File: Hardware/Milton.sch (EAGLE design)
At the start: 80 parts, among them Q1 12MHz, U10 MAX31850K, U2 DDC113TU-7-F, U3 USD-SOCKETNEW, U4 MMA8452Q, U5 TCR2EE50,LM, U6 SI4464, U7 TPS61200, U8 BME280, X1 B4B-ZR, X2 M023.5MM

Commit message: Update
Continue cleaning up traces and adding part numbers
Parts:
- removed C46: 100pF, SparkFun-Capacitors:CAP0603-CAP
- removed C47: 0.1uF, SparkFun-Capacitors:CAP0603-CAP
- removed C48: 1uF, SparkFun-Capacitors:CAP0603-CAP
- removed JP5: M02JST-PTH-2, SparkFun-Connectors:M02JST-PTH-2
- removed L8: SRN3015-2R2M, wrea:SRN3015-2R2M
- removed R15: 4.7k, SparkFun-Resistors:RESISTOR0603
- removed U$5: USB-CON-5PIN-105017-0001, GeekAmmo:USB-CON-5PIN-105017-0001
- added C21: 0.1uF, SparkFun-Capacitors:CAP0805
- added C33: 36pF, SparkFun-Capacitors:CAP0603-CAP
- added C34: 1000pF, SparkFun:CAP0805
- added JP2: (no value), SparkFun-Connectors:M03PTH
- added L3: 220nH, SparkFun-Passives:INDUCTOR0603
- added R12: 1k, SparkFun-Resistors:RESISTOR0603
- added U9: BME280, wrea:BME280
- C1: value 0.1uF -> 47pF; device SparkFun-Capacitors:CAP0805 -> SparkFun-Capacitors:CAP0603-CAP; MPN CL10B104KO8NNNC -> CL10C470JB8NCNC
- C10: value 0.1uF -> 10uF; device SparkFun-Capacitors:CAP0603-CAP -> SparkFun-Capacitors:10UF-TANT; MPN CL10B104KO8NNNC -> F931A106KAA
- C11: device SparkFun-Capacitors:CAP0603-CAP -> SparkFun:CAP0603-CAP
- C12: device SparkFun-Capacitors:10UF-TANT -> SparkFun-Capacitors:CAP0805; MPN F931A106KAA -> GRM21BR61C106KE15L
- C13: device SparkFun-Capacitors:CAP0805 -> SparkFun-Capacitors:CAP0603-CAP
- C14: value 100pF -> 10uF; device SparkFun-Capacitors:CAP0603-CAP -> SparkFun-Capacitors:CAP0805; MPN CL10B101KB8NNNC -> GRM21BR61C106KE15L
- C15: value 56pF -> 0.1uF; MPN CL10C560JB8NNNC -> CL10B104KO8NNNC
- C16: value 36pF -> 0.1uF; MPN GRM1885C1H360JA01D -> CL10B104KO8NNNC
- C17: value 22pF -> 0.1uF; device SparkFun:CAP0805 -> SparkFun-Capacitors:CAP0805; MPN C1608C0G1H220J080AA -> CL10B104KO8NNNC
- C18: value 10uF -> 4.7uF; device SparkFun-Capacitors:CAP0805 -> SparkFun-Capacitors:CAP0603-CAP; MPN GRM21BR61C106KE15L -> CC0603KRX5R6BB475
- C19: device SparkFun-Capacitors:CAP0603-CAP -> SparkFun-Capacitors:CAP0805
- C2: value 56pF -> 47pF; MPN CL10C560JB8NNNC -> CL10C470JB8NCNC
- C20: value 10uF -> 0.1uF; MPN GRM21BR61C106KE15L -> CL10B104KO8NNNC
- C22: value 0.1uF -> 100pF; MPN CL10B104KO8NNNC -> CL10B101KB8NNNC
- C23: value 1000pF -> 1uF; device SparkFun:CAP0805 -> SparkFun-Capacitors:CAP0603-CAP; MPN C0603C102J5RACTU -> CL10B105KP8NNNC
- C24: value 1000pF -> 0.1uF; MPN C0603C102J5RACTU -> CL10B104KO8NNNC
- C25: value 47pF -> 100pF; MPN CL10C470JB8NCNC -> CL10B101KB8NNNC
- C26: value 47pF -> 22pF; device SparkFun-Capacitors:CAP0603-CAP -> SparkFun:CAP0805; MPN CL10C470JB8NCNC -> C1608C0G1H220J080AA
- C27, C28: value 0.1uF -> 1000pF; device SparkFun-Capacitors:CAP0805 -> SparkFun-Capacitors:CAP0603-CAP; MPN CL10B104KO8NNNC -> C0603C102J5RACTU
- C29: value 4.7uF -> 12pF; MPN CC0603KRX5R6BB475 -> CL10C120JB8NNNC
- C3: device SparkFun:CAP0603-CAP -> SparkFun-Capacitors:CAP0603-CAP
- C30: value 12pF -> 36pF; MPN CL10C120JB8NNNC -> GRM1885C1H360JA01D
- C31: value 1000pF -> 56pF; MPN C0603C102J5RACTU -> CL10C560JB8NNNC
- C32: value 0.1uF -> 56pF; MPN CL10B104KO8NNNC -> CL10C560JB8NNNC
- C4: value 36pF -> 18pF; device SparkFun-Capacitors:CAP0603-CAP -> SparkFun-Capacitors:CAP0805; MPN GRM1885C1H360JA01D -> C0603C180K3GACTU
- C6: value 18pF -> 0.1uF; device SparkFun-Capacitors:CAP0805 -> SparkFun-Capacitors:CAP0603-CAP; MPN C0603C180K3GACTU -> CL10B104KO8NNNC
- FB1, FB2: value (none) -> FB; device LoganSmith-Inductors:FB-1K-100MHZ-0603 -> SparkFun-Passives:FB; MPN (none) -> BLM18PG471SN1D
- JP1: value (none) -> M02JST-PTH-2; device SparkFun-Connectors:M04PTH -> SparkFun-Connectors:M02JST-PTH-2; MPN (none) -> S2B-PH-K-S(LF)(SN)
- JP3: device SparkFun-Connectors:M03PTH -> SparkFun-Connectors:M04PTH
- L1: value 68nH -> SRN3015-2R2M; device SparkFun-Passives:INDUCTOR0603 -> wrea:SRN3015-2R2M; MPN LQW18AN68NG00D -> SRN3015-4R7M
- L2: value 72nH -> 470nH; MPN LQW18AN72NG00D -> L0603CR47JRMST
- L4: value 68nH -> 150nH; MPN LQW18AN68NG00D -> LQW18ANR15G00D
- L5: value 470nH -> 68nH; MPN L0603CR47JRMST -> LQW18AN68NG00D
- L6: value 220nH -> 72nH; MPN LQW18ANR22G00D -> LQW18AN72NG00D
- L7: value 150nH -> 68nH; MPN LQW18ANR15G00D -> LQW18AN68NG00D
- R1: value 27 -> 4.7k; MPN MCR03ERTJ270 -> ESR03EZPJ472
- R11: value 180k -> 4.7k; MPN RC1608F184CS -> ERJ-3GEYJ472V
- R2: value 27 -> 10k; MPN MCR03ERTJ270 -> ESR03EZPJ103
- R3: value 4.7k -> 27; MPN ESR03EZPJ472 -> MCR03ERTJ270
- R4: value 1k -> 27; MPN RMCF0603JT1K00 -> MCR03ERTJ270
- R5: value 4.7k -> 10K; MPN ERJ-3GEYJ472V -> ESR03EZPJ103
- R6: value 4.7k -> 1M; MPN ERJ-3GEYJ472V -> MCT06030C1004FP500
- R7: value 10k -> 180k; MPN ESR03EZPJ103 -> RC1608F184CS
- R8: value 10K -> 4.7k; MPN ESR03EZPJ103 -> ERJ-3GEYJ472V
- R9: value 1M -> 4.7k; MPN MCT06030C1004FP500 -> ERJ-3GEYJ472V
- U$1: value 1575AT43A40 -> USB-MICRO_105017-0001; device ava:JTI_ANTENNA-1575AT43A40 -> wrea:USB-MICRO_105017-0001; MPN 1575AT43A0040E -> 105017-0001
- U$2: value UBLOX_MAX -> 1575AT43A40; device ava:UBLOX_MAX -> ava:JTI_ANTENNA-1575AT43A40; MPN MAX-7C-0 -> 1575AT43A0040E
- U$3: value FT231XQ-R -> UBLOX_MAX; device ftdi_ft231xq-r:FT231XQ-R -> ava:UBLOX_MAX; MPN (none) -> MAX-7C-0
- U1: value (none) -> FT231X; device microbuilder:LPC1768 -> wrea:FT231X; MPN LPC1768FBD100,551 -> FT231XQ-R
- U10: value MAX31850K -> SI4464; device LoganSmith-Analog_IC:MAX31850K -> ava:SI4464; MPN MAX31850TATB+ -> SI4464-B1B-FM
- U2: value DDC113TU-7-F -> (none); device wrea:DDC113TU-7-F -> microbuilder:LPC1768; MPN DDC113TU-7-F -> LPC1768FBD100,551
- U4: value MMA8452Q -> DDC113TU-7-F; device SparkFun-Sensors:MMA8452Q -> wrea:DDC113TU-7-F; MPN MMA8452QT -> DDC113TU-7-F
- U5: value TCR2EE50,LM -> TPS61200; device Xevelabs:IC_TCR2EEESV -> texas:TPS61200; MPN (none) -> TPS61200DRCR
- U6: value SI4464 -> TCR2EE50,LM; device ava:SI4464 -> Xevelabs:IC_TCR2EEESV; MPN SI4464-B1B-FM -> (none)
- U7: value TPS61200 -> MMA8452Q; device texas:TPS61200 -> SparkFun-Sensors:MMA8452Q; MPN TPS61200DRCR -> MMA8452QT
- U8: value BME280 -> MAX31850K; device wrea:BME280 -> LoganSmith-Analog_IC:MAX31850K; MPN (none) -> MAX31850TATB+
- X2: MPN (none) -> ED555/2DS
- renumbered J$3 to J$1, R18 to R13
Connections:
- removed net RSTOUT: U1.RSTOUT
- removed net RTCK: U1.RTCK
- removed net RXD1: U$2.2_TXD1, U1.P2[1]/PWM1[2]/RXD1
- removed net TCK: U1.TCK/SWDCLK
- removed net TDI: U1.TDI
- removed net TDO: U1.TDO/SWO
- removed net TMS: U1.TMS/SWDIO
- removed net TXD1: U$2.3_RXD1, U1.P2[0]/PWM1[1]/TXD1
- net 3.3V: now also C10.+, C11.1, C14.1, C16.1, C17.1, C18.1, C21.1, C23.1, C24.1, C25.1, C27.2, C6.2, C7.2, JP2.3, JP3.4, L2.1, R11.2, U$3.6_V_BCKP, U$3.7_VCC_IO, U$3.8_VCC, U$3.9_V_RESET, U1.VCC, U10.VDD2, U2.VBAT, U2.VDD(3V3)1, U2.VDD(3V3)2, U2.VDD(3V3)3, U2.VDD(3V3)4, U2.VDD(REG)(3V3)1, U2.VDD(REG)(3V3)2, U2.VDDA, U2.VREFP, U5.VOUT, U6.VIN, U7.VDD, U7.VDDIO, U9.VDD, U9.VDDIO; no longer C1.1, C10.2, C11.2, C12.+, C20.1, C24.2, C28.1, C29.1, C3.1, C32.1, C46.1, C47.1, C48.1, JP1.4, JP3.3, L5.1, R15.2, U$2.6_V_BCKP, U$2.7_VCC_IO, U$2.8_VCC, U$2.9_V_RESET, U$3.VCC, U1.VBAT, U1.VDD(3V3)1, U1.VDD(3V3)2, U1.VDD(3V3)3, U1.VDD(3V3)4, U1.VDD(REG)(3V3)1, U1.VDD(REG)(3V3)2, U1.VDDA, U1.VREFP, U4.VDD, U4.VDDIO, U5.VIN, U6.VDD, U6.VDD2, U7.VOUT, U8.VDDIO
- net 5V: now also C15.1, U4G$1.C, U4G$2.C, U6.VOUT; no longer C22.1, U2G$1.C, U2G$2.C, U5.VOUT
- net 5V_EN: now also U2.P1[25]/MC1A/MAT1[1], U6.EN; no longer U1.P1[25]/MC1A/MAT1[1], U5.EN
- net ADC_IN1: now also JP3.2, U2.P0[23]/AD0[0]/I2SRX_CLK/CAP3[0]; no longer JP1.2, U1.P0[23]/AD0[0]/I2SRX_CLK/CAP3[0]
- net ADC_IN2: now also U2.P0[24]/AD0[1]/I2SRX_WS/CAP3[1]; no longer U1.P0[24]/AD0[1]/I2SRX_WS/CAP3[1]
- net CAM1: now also U4G$1.E; no longer U2G$1.E
- net CAM2: now also U4G$2.E; no longer U2G$2.E
- net CAMERA1_EN: now also U2.P1[26]/MC1B/PWM1[6]/CAP0[0], U4G$1.B; no longer U1.P1[26]/MC1B/PWM1[6]/CAP0[0], U2G$1.B
- net CAMERA2_EN: now also U2.P1[24]/MCFB2/PWM1[5]/MOSI0, U4G$2.B; no longer U1.P1[24]/MCFB2/PWM1[5]/MOSI0, U2G$2.B
- net DAC: now also U2.P0[26]/AD0[3]/AOUT/RXD3; no longer U1.P0[26]/AD0[3]/AOUT/RXD3
- net DIGITAL_1: now also JP2.1, U2.P2[2]/PWM1[3]/CTS1/TRACEDATA[3]; no longer JP3.1, U1.P2[2]/PWM1[3]/CTS1/TRACEDATA[3]
- net DIGITAL_2: now also JP3.1, U2.P0[25]/AD0[2]/I2SRX_SDA/TXD3; no longer JP1.1, U1.P0[25]/AD0[2]/I2SRX_SDA/TXD3
- net EINT1: now also U2.P2[11]/EINT1/I2STX_CLK, U7.INT1; no longer U1.P2[11]/EINT1/I2STX_CLK, U4.INT1
- net EXT_TEMP: now also U2.P0[11]/RXD2/SCL2/MAT3[1], U8.DQ; no longer U1.P0[11]/RXD2/SCL2/MAT3[1], U10.DQ
- net GND: now also C1.1, C10.-, C11.2, C12.2, C13.2, C14.2, C17.2, C21.2, C23.2, C24.2, C27.1, C30.2, C31.2, C33.2, C6.1, C7.1, JP1.1, JP2.2, JP3.3, R12.1, R2.1, U$1.GND, U$3.1_GND, U$3.4_TIMEPULSE, U1.GND_PIN13, U1.GND_PIN21, U1.GND_PIN3, U10.GND2, U2.VREFN, U2.VSS1, U2.VSS2, U2.VSS3, U2.VSS4, U2.VSS5, U2.VSS6, U2.VSSA, U5.PGND, U5.PP, U5.PP@1, U5.PP@2, U7.GND@0, U7.GND@1, U7.GND@2, U7.SA0, U8.AD0, U8.AD1, U8.AD2, U8.AD3, U8.PAD, U9.GND, U9.SDO; no longer C1.2, C10.1, C11.1, C12.-, C17.1, C20.2, C22.2, C24.1, C27.2, C28.2, C29.2, C46.2, C47.2, C48.2, C6.2, C7.2, JP1.3, JP3.2, JP5.1, R11.1, R4.1, U$2.1_GND, U$2.4_TIMEPULSE, U$3.GND_PIN13, U$3.GND_PIN21, U$3.GND_PIN3, U$5.GND, U1.VREFN, U1.VSS1, U1.VSS2, U1.VSS3, U1.VSS4, U1.VSS5, U1.VSS6, U1.VSSA, U10.AD0, U10.AD1, U10.AD2, U10.AD3, U10.PAD, U4.GND@0, U4.GND@1, U4.GND@2, U4.SA0, U6.GND2, U7.GND, U7.PGND, U7.PP, U7.PP@1, U7.PP@2, U8.SDO
- net IC6_RTC1: now also C4.1, U2.XTAL1; no longer C5.1, U1.XTAL1
- net IC6_RTC2: now also C5.1, U2.XTAL2; no longer C6.1, U1.XTAL2
- net ISP_BOOT: now also U1.RTS#, U2.P2[10]/EINT0/NMI; no longer U$3.RTS#, U1.P2[10]/EINT0/NMI
- net N$1: now also R6.1, R7.2, U5.FB; no longer R11.2, R9.1, U7.FB
- net N$10: now also R1.2, U$1.VBUS; no longer R3.2, U$5.VBUS
- net N$11: now also C32.1, L6.1, L7.2; no longer C15.1, L2.1, L4.2
- net N$12: now also C3.1, U1.3V3OUT, U1.RESET#, U1.VCCIO; no longer C7.1, U$3.3V3OUT, U$3.RESET#, U$3.VCCIO
- net N$18: now also C28.2, L2.2, U10.TX; no longer C31.2, L5.2, U6.TX
- net N$19: now also L1.1, U5.L; no longer L8.1, U7.L
- net N$2: now also C19.1, U7.BYP; no longer C27.1, U4.BYP
- net N$20: now also C29.2, L3.2, U10.RXN; no longer C30.2, L6.2, U6.RXN
- net N$21: now also R1.1, R2.2, U1.CBUS0; no longer R3.1, R7.2, U$3.CBUS0
- net N$28: now also C22.2; no longer C14.2
- net N$29: now also C26.2, L3.1, L4.2, U10.RXP; no longer C17.2, L6.1, L7.2, U6.RXP
- net N$30: now also C33.1, C34.2, L7.1; no longer C16.1, C23.2, L4.1
- net N$33: now also C34.1; no longer C23.1
- net N$36: now also C28.1, C29.1, L4.1, L5.2; no longer C31.1, C4.1, L1.2, L7.1
- net N$37: now also C31.1, L5.1, L6.2; no longer C2.1, L1.1, L2.2
- net N$38: now also U10.XIN; no longer U6.XIN
- net N$4: now also C2.1, R3.2, U1.USBDP; no longer C25.1, R1.2, U$3.USBDP
- net N$5: now also R4.2, U1.USBDM; no longer R2.2, U$3.USBDM
- net N$6: now also C22.1, U10.XOUT; no longer C14.1, U6.XOUT
- net N$7: now also R3.1, U$1.D+; no longer R1.1, U$5.D+
- net N$8: now also U$2.FEED, U$3.11_RF_IN; no longer U$1.FEED, U$2.11_RF_IN
- net N$9: now also C1.2, R4.1, U$1.D-; no longer C26.2, R2.1, U$5.D-
- net RADIO_EN: now also U10.SDN; no longer U6.SDN
- net RADIO_SEL: now also U10.NSEL, U2.P2[9]/USB_CONNECT/RXD2; no longer U1.P2[9]/USB_CONNECT/RXD2, U6.NSEL
- net RESET: now also R5.1, U1.DTR#, U2.RESET; no longer R8.1, U$3.DTR#, U1.RESET
- net RF_MISO: now also U10.SDO, U2.P0[17]/CTS1/MISO0/MISO; no longer U1.P0[17]/CTS1/MISO0/MISO, U6.SDO
- net RF_MOSI: now also U10.SDI, U2.P0[18]/DCD1/MOSI0/MOSI; no longer U1.P0[18]/DCD1/MOSI0/MOSI, U6.SDI
- net RF_NIRQ: now also U10.NIRQ, U2.P0[16]/RXD1/SSEL0/SSEL; no longer U1.P0[16]/RXD1/SSEL0/SSEL, U6.NIRQ
- net RF_SCK: now also U10.SCLK, U2.P0[15]/TXD1/SCK0/SCK; no longer U1.P0[15]/TXD1/SCK0/SCK, U6.SCLK
- net RXD0: now also U$3.2_TXD1, U1.TXD, U2.P0[3]/RXD0/AD0[6]; no longer U$3.TXD, U1.P0[3]/RXD0/AD0[6]
- net SCL0: now also R8.1, U2.P0[28]/SCL0/USB_SCL, U7.SCL; no longer R5.1, U1.P0[28]/SCL0/USB_SCL, U4.SCL
- net SCL1: now also R11.1, U2.P0[20]/DTR1/SCL1, U9.SCL; no longer R10.1, U1.P0[20]/DTR1/SCL1, U8.SCL
- net SDA0: now also R9.1, U2.P0[27]/SDA0/USB_SDA, U7.SDA; no longer R6.1, U1.P0[27]/SDA0/USB_SDA, U4.SDA
- net SDA1: now also R10.1, U2.P0[19]/DSR1/SDA1, U9.SDA; no longer R15.1, U1.P0[19]/DSR1/SDA1, U8.SDA
- net SD_CS: now also U2.P0[6]/I2SRX_SDA/SSEL1/MAT2[0]; no longer U1.P0[6]/I2SRX_SDA/SSEL1/MAT2[0]
- net SD_MISO: now also U2.P0[8]/I2STX_WS/MISO1/MAT2[2]; no longer U1.P0[8]/I2STX_WS/MISO1/MAT2[2]
- net SD_MOSI: now also U2.P0[9]/I2STX_SDA/MOSI1/MAT2[3]; no longer U1.P0[9]/I2STX_SDA/MOSI1/MAT2[3]
- net SD_SCK: now also U2.P0[7]/I2STX_CLK/SCK1/MAT2[1]; no longer U1.P0[7]/I2STX_CLK/SCK1/MAT2[1]
- net TM_FILT: now also C20.2, FB2.P$1, U8.T-; no longer C13.2, FB2.2, U10.T-
- net TM_RAW: now also FB2.P$2; no longer FB2.1
- net TP_FILT: now also C20.1, FB1.P$1, U8.T+; no longer C13.1, FB1.2, U10.T+
- net TP_RAW: now also FB1.P$2; no longer FB1.1
- net TRST: now also U2.TRST; no longer U1.TRST
- net TXD0: now also U$3.3_RXD1, U1.RXD, U2.P0[2]/TXD0/AD0[7]; no longer U$3.RXD, U1.P0[2]/TXD0/AD0[7]
- net VAUX: now also C13.1, U5.VAUX; no longer C19.1, U7.VAUX
- net VIN: now also C12.1, JP1.2, L1.2, U5.EN, U5.PS, U5.UVLO, U5.VIN; no longer C18.1, JP5.2, L8.2, U7.EN, U7.PS, U7.UVLO, U7.VIN
- net XTAL_EN: now also R12.2, U2.P0[21]/RI1/RD1; no longer R4.2, U1.P0[21]/RI1/RD1

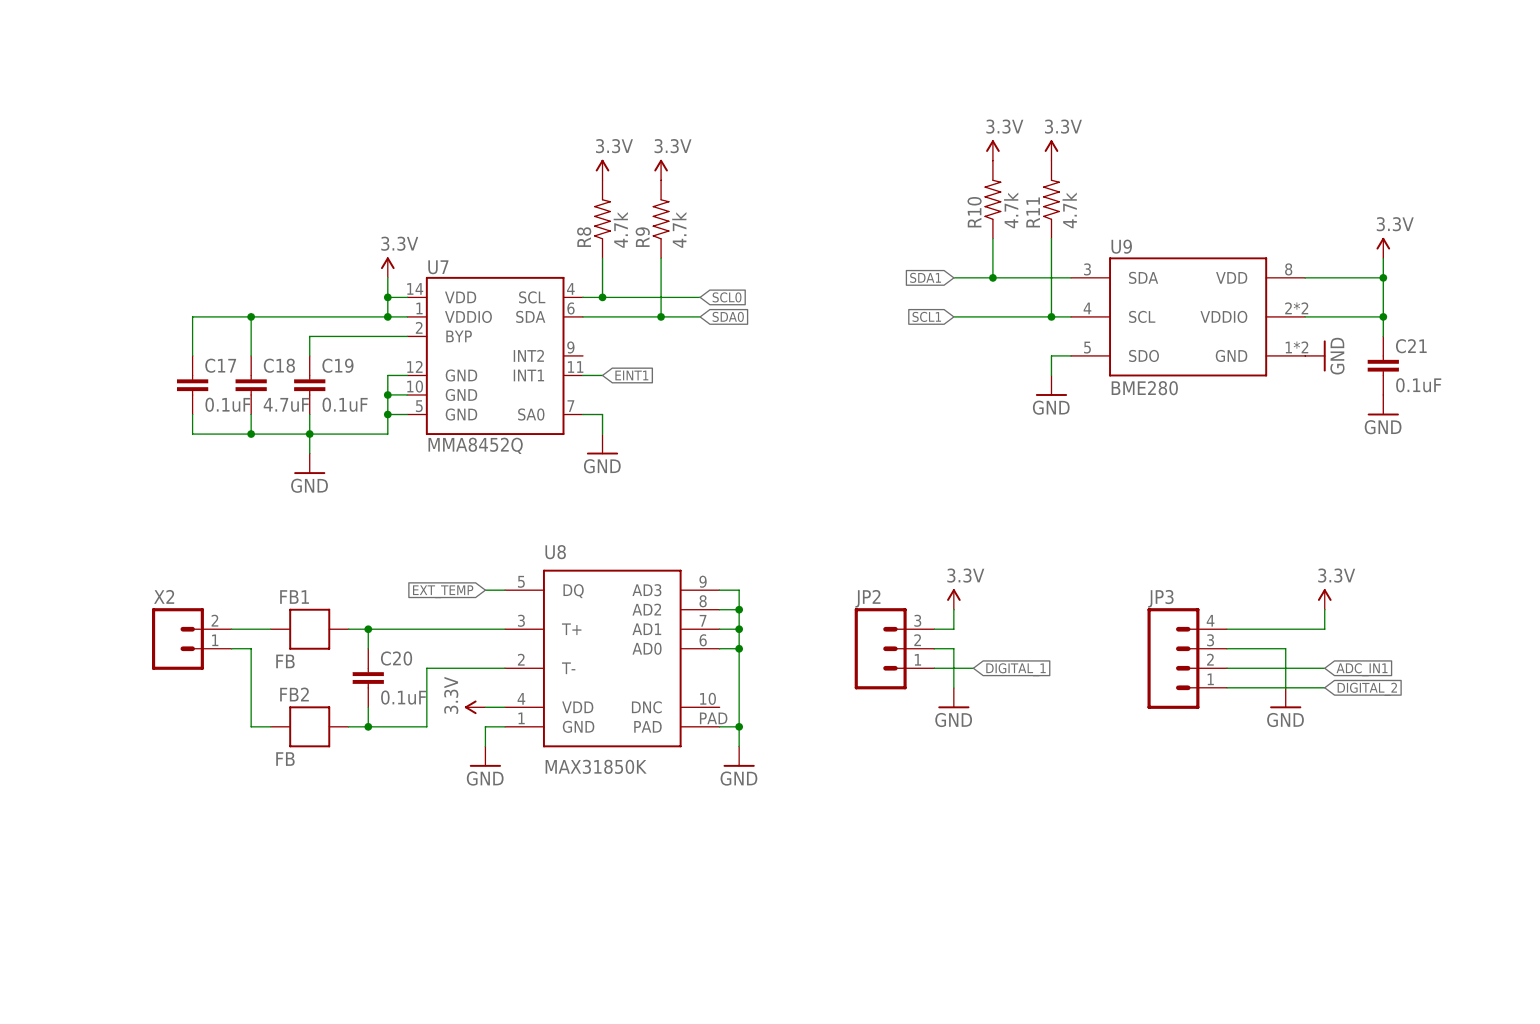
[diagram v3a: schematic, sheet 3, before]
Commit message: Cleanup
Cleaning up layout. Optimizing traces by changing pins used.
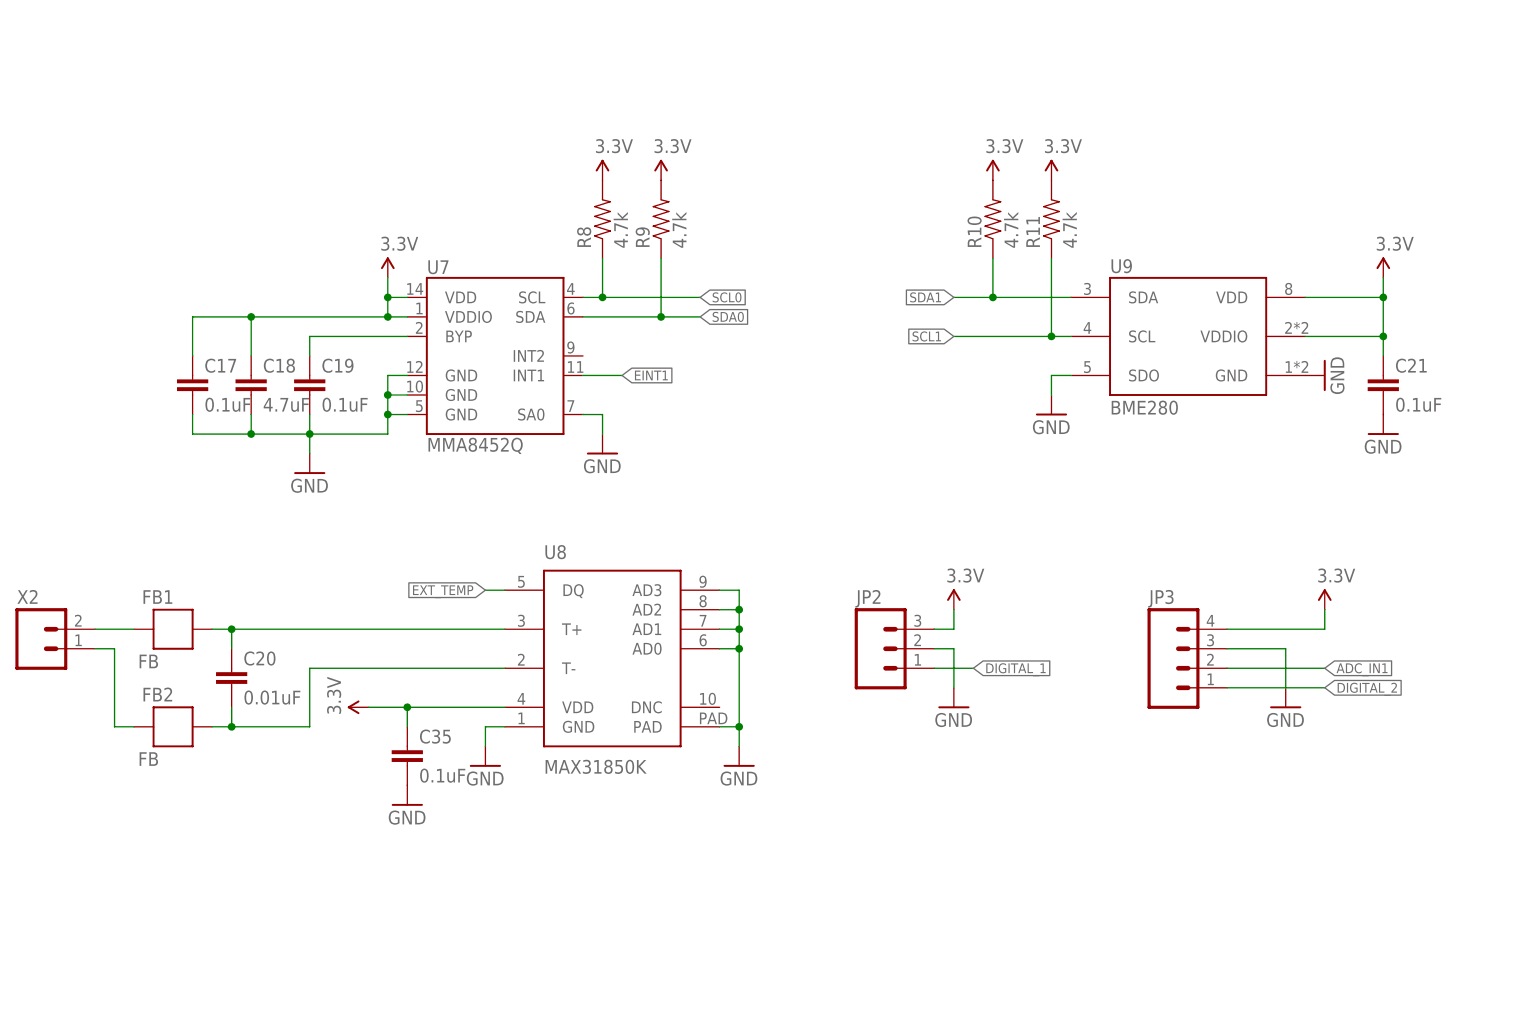
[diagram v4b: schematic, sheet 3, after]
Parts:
- added C35: 0.1uF, SparkFun-Capacitors:CAP0805
- C20: value 0.1uF -> 0.01uF; MPN CL10B104KO8NNNC -> C0603C103J5RACTU
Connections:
- net 3.3V: now also C35.1
- net CAMERA1_EN: now also U2.P3[26]/STCLK/MAT0[1]/PWM1[3]; no longer U2.P1[26]/MC1B/PWM1[6]/CAP0[0]
- net GND: now also C35.2
- net XTAL_EN: now also U2.P2[0]/PWM1[1]/TXD1; no longer U2.P0[21]/RI1/RD1
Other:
- moved on the sheet: C12, C20, C21, FB1, FB2, JP1, R10, R11, R6, R7, U9, X2

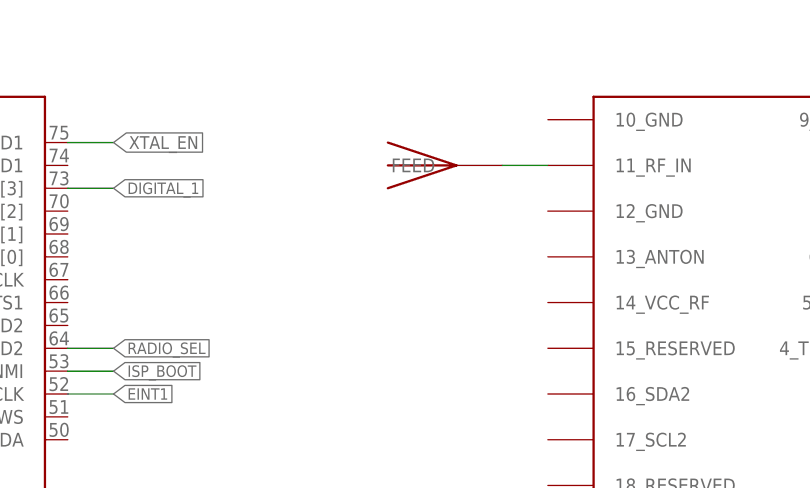
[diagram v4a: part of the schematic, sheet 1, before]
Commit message: Fix
Forgot to connect pins 10 & 12 of ublox to GND
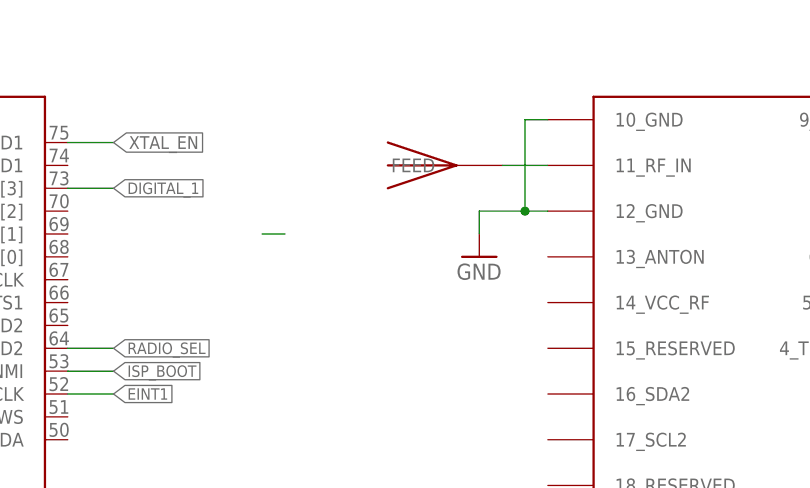
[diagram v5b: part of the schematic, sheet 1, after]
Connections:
- net GND: now also U$3.10_GND, U$3.12_GND
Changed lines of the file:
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@@
 </part>
 <part name="GND36" library="SparkFun" deviceset="GND" device=""/>
+<part name="GND37" library="SparkFun" deviceset="GND" device=""/>
 </parts>
 <sheets>
@@
 <attribute name="MPN" x="27.94" y="101.6" size="1.27" layer="96" display="off"/>
 </instance>
+<instance part="GND37" gate="1" x="317.5" y="175.26"/>
 </instances>
 <busses>
@@
 <pinref part="GND9" gate="1" pin="GND"/>
 </segment>
+<segment>
+<pinref part="U$3" gate="G$1" pin="10_GND"/>
+<wire x1="325.12" y1="190.5" x2="322.58" y2="190.5" width="0.1524" layer="91"/>
+<wire x1="322.58" y1="190.5" x2="322.58" y2="180.34" width="0.1524" layer="91"/>
+<pinref part="U$3" gate="G$1" pin="12_GND"/>
+<wire x1="322.58" y1="180.34" x2="325.12" y2="180.34" width="0.1524" layer="91"/>
+<wire x1="317.5" y1="177.8" x2="317.5" y2="180.34" width="0.1524" layer="91"/>
+<wire x1="317.5" y1="180.34" x2="322.58" y2="180.34" width="0.1524" layer="91"/>
+<junction x="322.58" y="180.34"/>
+<pinref part="GND37" gate="1" pin="GND"/>
+</segment>
+<segment>
+<wire x1="295.91" y1="177.8" x2="293.37" y2="177.8" width="0.1524" layer="91"/>
+</segment>
 </net>

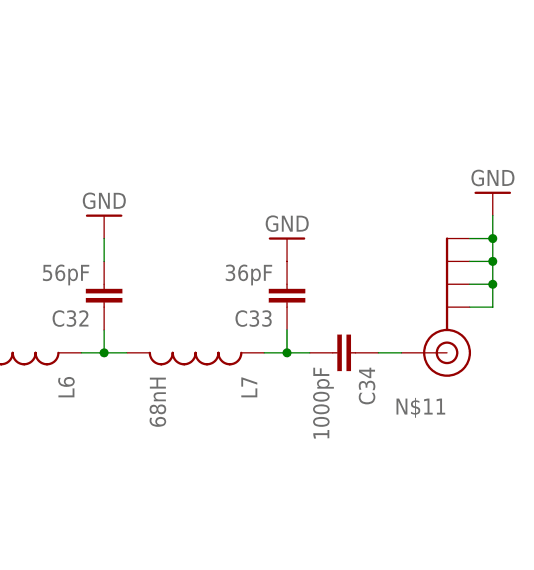
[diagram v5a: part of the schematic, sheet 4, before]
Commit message: Change SMA connector
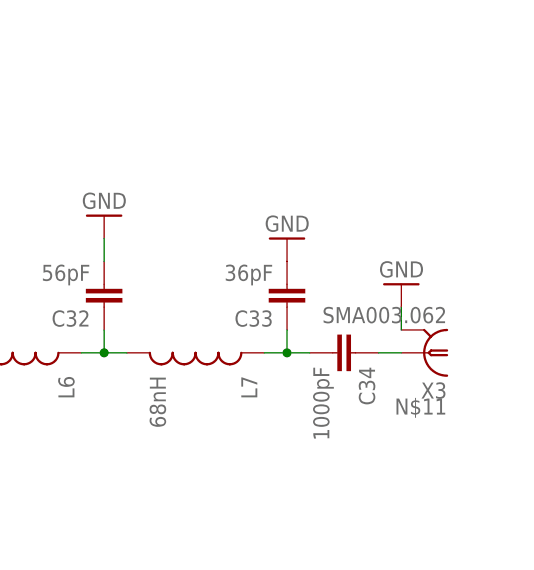
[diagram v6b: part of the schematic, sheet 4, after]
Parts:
- removed J$1: SMA_EDGE, SparkFun:SMA_EDGE
- added X3: SMA003.062, wrea:SMA003.062
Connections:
- net GND: now also X3.2; no longer J$1.GND@0, J$1.GND@1, J$1.GND@2, J$1.GND@3
- net N$33: now also X3.1; no longer J$1.SIGNAL
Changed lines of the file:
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@@
 <attribute name="MPN" value="MCT06030C1003FP500"/>
 </part>
-<part name="J$1" library="SparkFun" deviceset="SMA_EDGE" device=""/>
 <part name="GND67" library="SparkFun" deviceset="GND" device=""/>
 <part name="GND14" library="SparkFun" deviceset="GND" device=""/>
@@
 <part name="GND36" library="SparkFun" deviceset="GND" device=""/>
 <part name="GND37" library="SparkFun" deviceset="GND" device=""/>
+<part name="X3" library="wrea" deviceset="SMA003.062" device=""/>
 </parts>
 <sheets>
@@
 <attribute name="MPN" x="205.74" y="-7.62" size="1.27" layer="96" display="off"/>
 </instance>
-<instance part="J$1" gate="1" x="325.12" y="15.24" rot="R180"/>
-<instance part="GND67" gate="1" x="330.2" y="33.02" rot="R180"/>
+<instance part="GND67" gate="1" x="320.04" y="22.86" rot="R180"/>
 <instance part="GND14" gate="1" x="208.28" y="0"/>
 <instance part="SUPPLY14" gate="G$1" x="220.98" y="40.64" rot="R270"/>
@@
 <instance part="GND6" gate="1" x="111.76" y="-25.4"/>
 <instance part="SJ1" gate="G$1" x="175.26" y="-15.24"/>
+<instance part="X3" gate="A" x="322.58" y="15.24" rot="R180"/>
 </instances>
 <busses>
@@
 </segment>
 <segment>
-<pinref part="J$1" gate="1" pin="GND@0"/>
-<pinref part="GND67" gate="1" pin="GND"/>
-<wire x1="327.66" y1="20.32" x2="330.2" y2="20.32" width="0.1524" layer="91"/>
-<wire x1="330.2" y1="20.32" x2="330.2" y2="22.86" width="0.1524" layer="91"/>
-<pinref part="J$1" gate="1" pin="GND@3"/>
-<wire x1="330.2" y1="22.86" x2="330.2" y2="25.4" width="0.1524" layer="91"/>
-<wire x1="330.2" y1="25.4" x2="330.2" y2="27.94" width="0.1524" layer="91"/>
-<wire x1="330.2" y1="27.94" x2="330.2" y2="30.48" width="0.1524" layer="91"/>
-<wire x1="327.66" y1="27.94" x2="330.2" y2="27.94" width="0.1524" layer="91"/>
-<pinref part="J$1" gate="1" pin="GND@2"/>
-<wire x1="327.66" y1="25.4" x2="330.2" y2="25.4" width="0.1524" layer="91"/>
-<pinref part="J$1" gate="1" pin="GND@1"/>
-<wire x1="327.66" y1="22.86" x2="330.2" y2="22.86" width="0.1524" layer="91"/>
-<junction x="330.2" y="22.86"/>
-<junction x="330.2" y="25.4"/>
-<junction x="330.2" y="27.94"/>
-</segment>
-<segment>
 <pinref part="U10" gate="G$1" pin="GND"/>
 <wire x1="205.74" y1="5.08" x2="208.28" y2="5.08" width="0.1524" layer="91"/>
@@
 <pinref part="R12" gate="G$1" pin="1"/>
 <pinref part="GND6" gate="1" pin="GND"/>
+</segment>
+<segment>
+<pinref part="X3" gate="A" pin="2"/>
+<pinref part="GND67" gate="1" pin="GND"/>
+<wire x1="320.04" y1="17.78" x2="320.04" y2="20.32" width="0.1524" layer="91"/>
 </segment>
 </net>
@@
 <segment>
 <pinref part="C34" gate="G$1" pin="1"/>
-<pinref part="J$1" gate="1" pin="SIGNAL"/>
 <wire x1="317.5" y1="15.24" x2="320.04" y2="15.24" width="0.1524" layer="91"/>
-</segment>
-</net>
+<pinref part="X3" gate="A" pin="1"/>
+</segment>
+</net>

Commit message: Cleanup schematics
Cleanup schematics and added images
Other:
- note added: "1.0"
- note added: "BME280"
- note added: "Camera Triggers"
- note added: "Headers"
- note added: "LPC1768"
- note added: "MAX31850"
- note added: "MMA8452Q"
- note added: "Power Supplies"
- note added: "SD Card"
- note added: "SI4464 RF IC"
- note added: "USB-FTDI"
- note added: "ublox MAX GPS"
